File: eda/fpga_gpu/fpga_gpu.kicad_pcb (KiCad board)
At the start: 2 copper layers, 99.3 x 75.9 mm, 70 parts, among them J1 VGA, J2 Bus expansion, J3 programming, J4 reset ground, Q1 2N7002, SW1 SW_Reset, SW2 SW_FlashPwrCycle, U1 ICE40HX4K-TQ144, U10 IS61C5128AL-10KLI, U11 74HCT00, U2 SST25VF080B-50-4x-S2Ax, U3 74HCT541, U4 74HCT541, U5 74HCT541, U6 TXS0108EPW, U7 TXS0108EPW, U8 AMS1117-3.3, U9 AP2112K-1.2, X1 TXC-7C

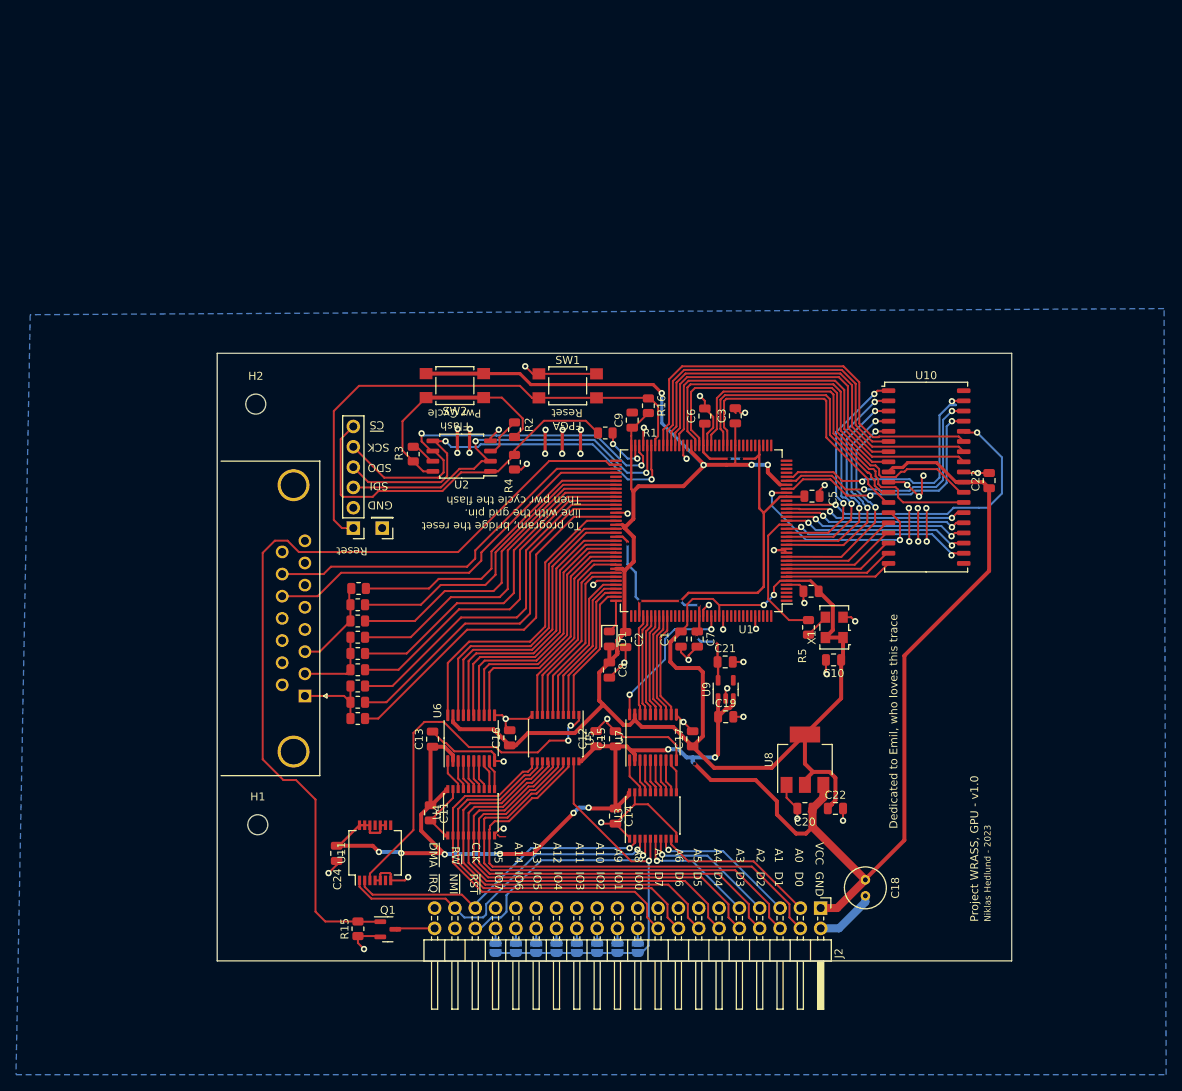
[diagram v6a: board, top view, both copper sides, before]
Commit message: Generate step files and start on gpu for new board layout
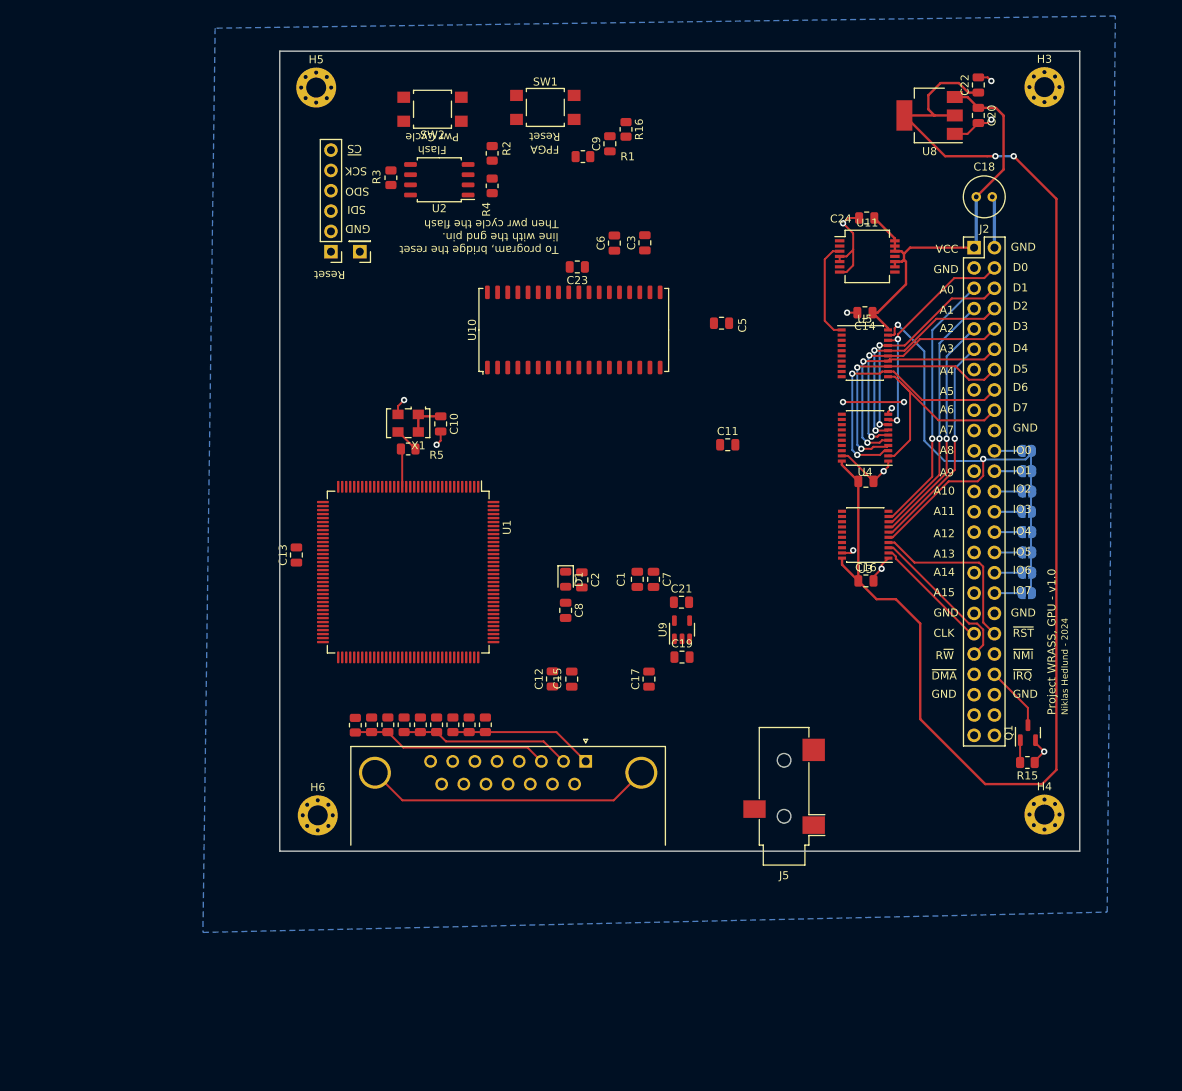
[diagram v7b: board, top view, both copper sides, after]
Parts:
- removed H1, H2: MountingHole, MountingHole:MountingHole_2.5mm
- removed U6, U7: TXS0108EPW, Package_SO:TSSOP-20_4.4x6.5mm_P0.65mm
- added H3: MountingHole_Pad, MountingHole:MountingHole_2.5mm_Pad_Via, F.Cu at (154.7, 43.2)
- added H4: MountingHole_Pad, MountingHole:MountingHole_2.5mm_Pad_Via, F.Cu at (154.7, 134.1)
- added H5: MountingHole_Pad, MountingHole:MountingHole_2.5mm_Pad_Via, F.Cu at (63.7, 43.2)
- added H6: MountingHole_Pad, MountingHole:MountingHole_2.5mm_Pad_Via, F.Cu at (63.9, 134.2)
- added J5: AudioPlug3, Connector_Audio:Jack_3.5mm_CUI_SJ-3523-SMT_Horizontal, F.Cu at (122.2, 131.8)
- J2: value Bus expansion -> Conn_02x25_Odd_Even; footprint Connector_PinHeader_2.54mm:PinHeader_2x20_P2.54mm_Horizontal -> Connector_PinHeader_2.54mm:PinHeader_2x25_P2.54mm_Vertical
- U3, U4: value 74HCT541 -> 74HC541
- moved C24 103.4 mm to (132.5, 59.5), turned to 180 degrees
- moved U11 96.7 mm to (132.6, 64.3), turned to 0 degrees
- moved C22 92.2 mm to (146.5, 42.9), turned to 90 degrees
- moved C20 89.3 mm to (146.5, 46.7), turned to -90 degrees
- moved C18 86.5 mm to (146.2, 56.9), turned to 0 degrees
- moved R15 86.2 mm to (152.6, 127.6), turned to 180 degrees
- moved J2 84.7 mm to (145.9, 63.2), turned to 0 degrees
- moved Q1 83.7 mm to (152.7, 123.9), turned to 90 degrees
- moved U8 82.0 mm to (140.4, 46.7), turned to 180 degrees
- moved JP8 79.8 mm to (152.5, 106.4), turned to 0 degrees
- moved JP7 79.2 mm to (152.5, 103.9), turned to 0 degrees
- moved JP1 78.9 mm to (152.5, 88.6), turned to 0 degrees
- moved JP6 78.8 mm to (152.5, 101.3), turned to 0 degrees
- moved JP2 78.6 mm to (152.5, 91.2), turned to 0 degrees
- moved JP5 78.5 mm to (152.5, 98.8), turned to 0 degrees
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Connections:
- J2 pad 11: /Interfacing/Expansion/A4 -> /Interfacing/Expansion/A3
- J2 pad 13: /Interfacing/Expansion/A5 -> /Interfacing/Expansion/A4
- J2 pad 15: /Interfacing/Expansion/A6 -> /Interfacing/Expansion/A5
- J2 pad 17: /Interfacing/Expansion/A7 -> /Interfacing/Expansion/A6
- J2 pad 19: /Interfacing/Expansion/A8 -> /Interfacing/Expansion/A7
- J2 pad 20: Net-(J2-Pin_20) -> GND
- J2 pad 21: /Interfacing/Expansion/A9 -> /Interfacing/Expansion/A8
- J2 pad 23: /Interfacing/Expansion/A10 -> /Interfacing/Expansion/A9
- J2 pad 25: /Interfacing/Expansion/A11 -> /Interfacing/Expansion/A10
- J2 pad 27: /Interfacing/Expansion/A12 -> /Interfacing/Expansion/A11
- J2 pad 29: /Interfacing/Expansion/A13 -> /Interfacing/Expansion/A12
- J2 pad 3: /Interfacing/Expansion/A0 -> GND
- J2 pad 31: /Interfacing/Expansion/A14 -> /Interfacing/Expansion/A13
- J2 pad 33: /Interfacing/Expansion/A15 -> /Interfacing/Expansion/A14
- J2 pad 35: /Interfacing/Clock-VCC -> /Interfacing/Expansion/A15
- J2 pad 36: /Interfacing/Expansion/~{RST} -> Net-(J2-Pin_36)
- J2 pad 37: /Interfacing/R~{W}-VCC -> GND
- J2 pad 38: /Interfacing/Expansion/~{NMI} -> GND
- J2 pad 39: /Interfacing/Expansion/~{DMA} -> /Interfacing/Clock-VCC
- J2 pad 40: /Interfacing/~{IRQ} -> /Interfacing/Expansion/~{RST}
- J2 pad 5: /Interfacing/Expansion/A1 -> /Interfacing/Expansion/A0
- J2 pad 7: /Interfacing/Expansion/A2 -> /Interfacing/Expansion/A1
- J2 pad 9: /Interfacing/Expansion/A3 -> /Interfacing/Expansion/A2
- JP1 pad 1: Net-(J2-Pin_20) -> Net-(J2-Pin_22)
- JP2 pad 1: Net-(J2-Pin_22) -> Net-(J2-Pin_24)
- JP3 pad 1: Net-(J2-Pin_24) -> Net-(J2-Pin_26)
- JP4 pad 1: Net-(J2-Pin_26) -> Net-(J2-Pin_28)
- JP5 pad 1: Net-(J2-Pin_28) -> Net-(J2-Pin_30)
- JP6 pad 1: Net-(J2-Pin_30) -> Net-(J2-Pin_32)
- JP7 pad 1: Net-(J2-Pin_32) -> Net-(J2-Pin_34)
- JP8 pad 1: Net-(J2-Pin_34) -> Net-(J2-Pin_36)
- U3 pad 11: Net-(U3-Y7) -> /Interfacing/ADev0
- U3 pad 12: Net-(U3-Y6) -> /Interfacing/ADev1
- U3 pad 13: Net-(U3-Y5) -> /Interfacing/ADev2
- U3 pad 14: Net-(U3-Y4) -> /Interfacing/ADev3
- U3 pad 15: Net-(U3-Y3) -> /Interfacing/~{CS}
- U3 pad 16: Net-(U3-Y2) -> /Interfacing/~{RST}
- U3 pad 17: Net-(U3-Y1) -> /Interfacing/R~{W}
- U3 pad 18: Net-(U3-Y0) -> /Interfacing/Clock
- U3 pad 20: VCC -> +3.3V
- U4 pad 11: Net-(U4-Y7) -> /DIn0
- U4 pad 12: Net-(U4-Y6) -> /DIn1
- U4 pad 13: Net-(U4-Y5) -> /DIn2
- U4 pad 14: Net-(U4-Y4) -> /DIn3
- U4 pad 15: Net-(U4-Y3) -> /DIn4
- U4 pad 16: Net-(U4-Y2) -> /DIn5
- U4 pad 17: Net-(U4-Y1) -> /DIn6
- U4 pad 18: Net-(U4-Y0) -> /DIn7
- U4 pad 20: VCC -> +3.3V
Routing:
- net VCC: track 223.6 -> 55.1 mm, vias 9 -> 0
- net GND: track 186.2 -> 58.1 mm, vias 53 -> 13
- net /FpgaIRQ: track 107.4 -> 2.81 mm
- net +1V2: track 77.1 -> 0.00 mm, vias 8 -> 0
- net +3.3V: track 255.6 -> 178.8 mm, vias 6 -> 2
- net ice40-CRESET: track 64.4 -> 0.00 mm
- net /~{RamOE}: track 53.1 -> 0.00 mm
- net ice40-SDO: track 52.3 -> 0.00 mm, vias 2 -> 0
- net /RamIo7: track 51.6 -> 0.00 mm
- net ice40-SCK: track 51.3 -> 0.00 mm, vias 2 -> 0
- net /RamIo5: track 50.9 -> 0.00 mm
- net /RamIo6: track 50.0 -> 0.00 mm
- net /VSYNC: track 48.7 -> 0.00 mm
- net ice40-SDI: track 48.5 -> 0.00 mm, vias 2 -> 0
- net /HSYNC: track 47.8 -> 0.00 mm
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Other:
- board size 99.3 x 75.9 mm -> 100 x 100 mm
- board text added: "Niklas Hedlund - 2024"
- board text removed: "Dedicated to Emil, who loves this trace"
- board text removed: "Niklas Hedlund - 2023"
